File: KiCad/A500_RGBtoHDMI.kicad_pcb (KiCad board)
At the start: 2 copper layers, 80 x 29.5 mm, 13 parts, among them J1 Conn_02x20_Odd_Even, U1 Denise_Socket, U2 XC9572XL-VQ64, U3 LM1117-3.3, U4 Denise_MB_PinHeader

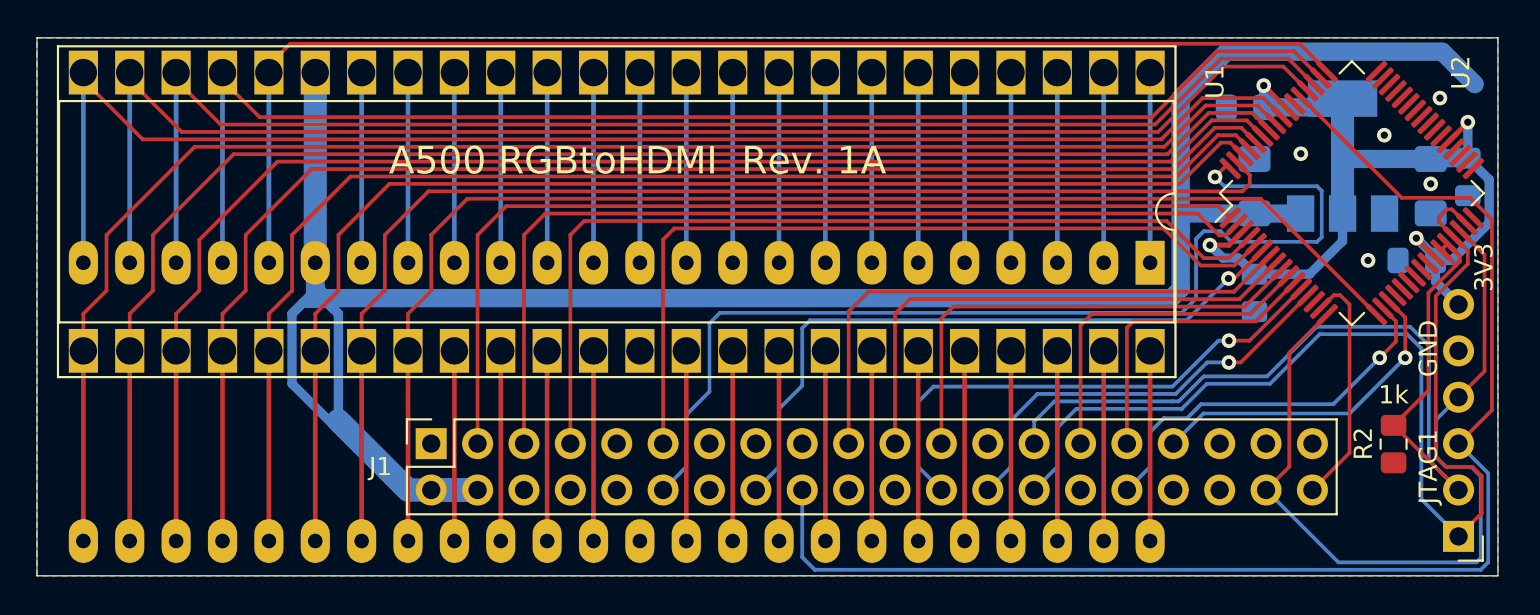
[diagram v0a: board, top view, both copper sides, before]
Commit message: added a two-pin power header VCC/GND
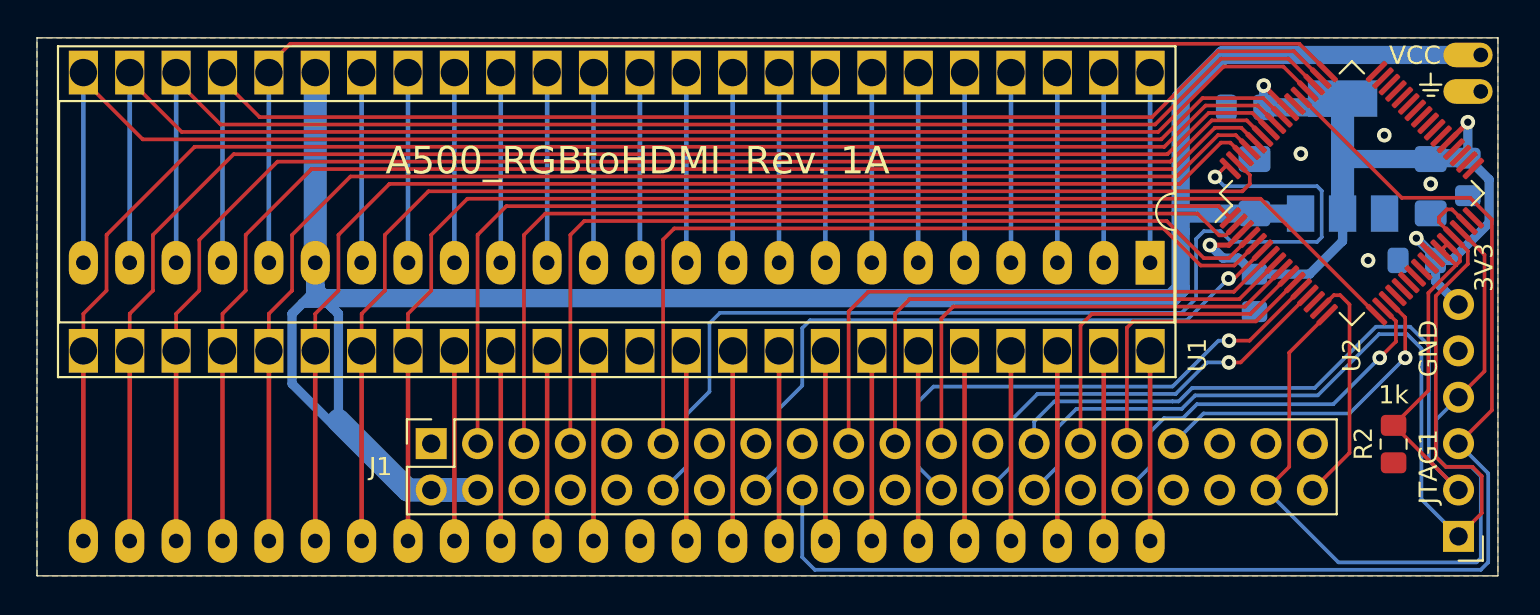
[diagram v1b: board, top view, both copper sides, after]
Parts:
- added J2: Conn_01x02, Connector_PinHeader_2.00mm:PinHeader_1x02_P2.00mm_Vertical, F.Cu at (206.1, 76.8)
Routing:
- net GND: vias 5 -> 4
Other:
- board text added: "A500_RGBtoHDMI Rev. 1A"
- board text added: "VCC"
- board text removed: "A500 RGBtoHDMI Rev. 1A"

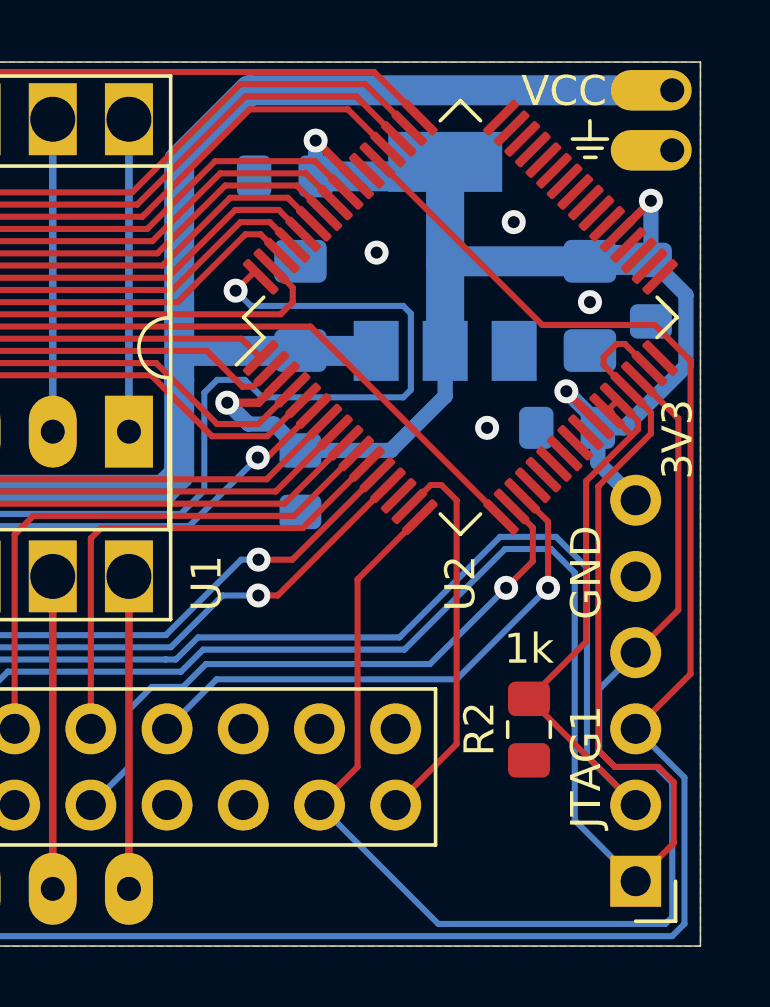
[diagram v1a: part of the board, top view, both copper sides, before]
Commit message: added Button-jumper (BT1) with 3V3-pull-up resistor
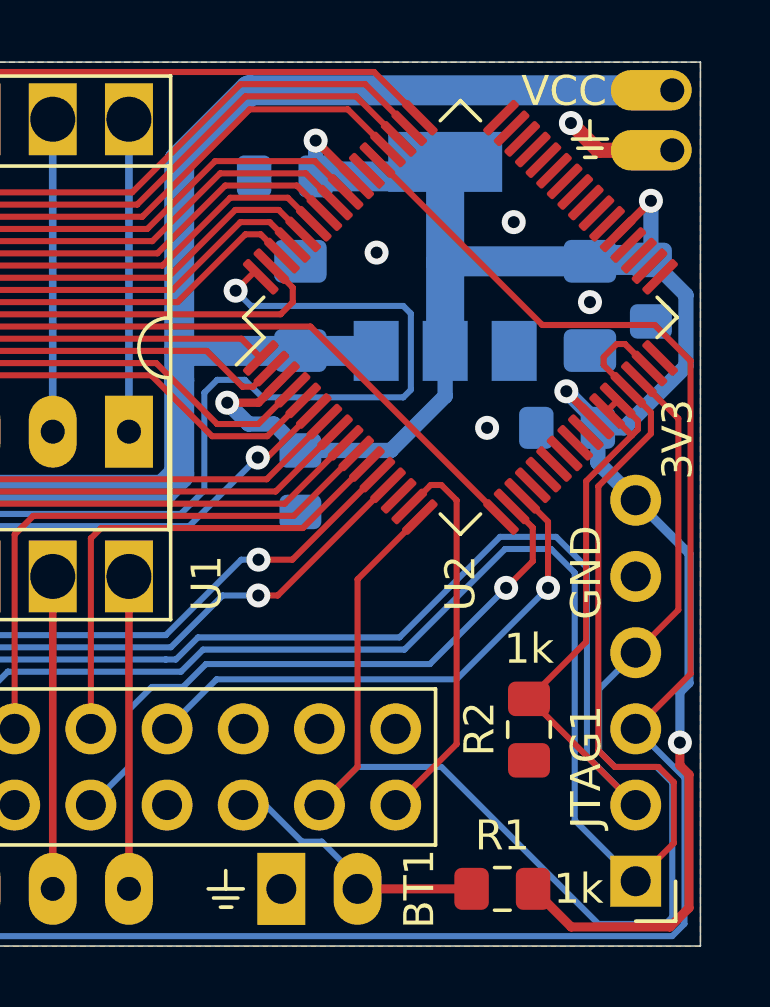
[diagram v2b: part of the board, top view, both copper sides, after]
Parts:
- added BT1: Jumper_2_Open, Connector_PinHeader_2.54mm:PinHeader_1x02_P2.54mm_Horizontal, B.Cu at (193.0, 103.4)
- added R1: 1k, Resistor_SMD:R_0805_2012Metric_Pad1.15x1.40mm_HandSolder, F.Cu at (200.4, 103.4)
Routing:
- net 3V3: track 50.5 -> 71.1 mm, vias 4 -> 5
- net Net-(BT1-Pad2): track 0.00 -> 8.99 mm
- net GND: track 0.00 -> 3.75 mm, vias 4 -> 5
- net TCK_SPCLK: track 45.9 -> 46.9 mm

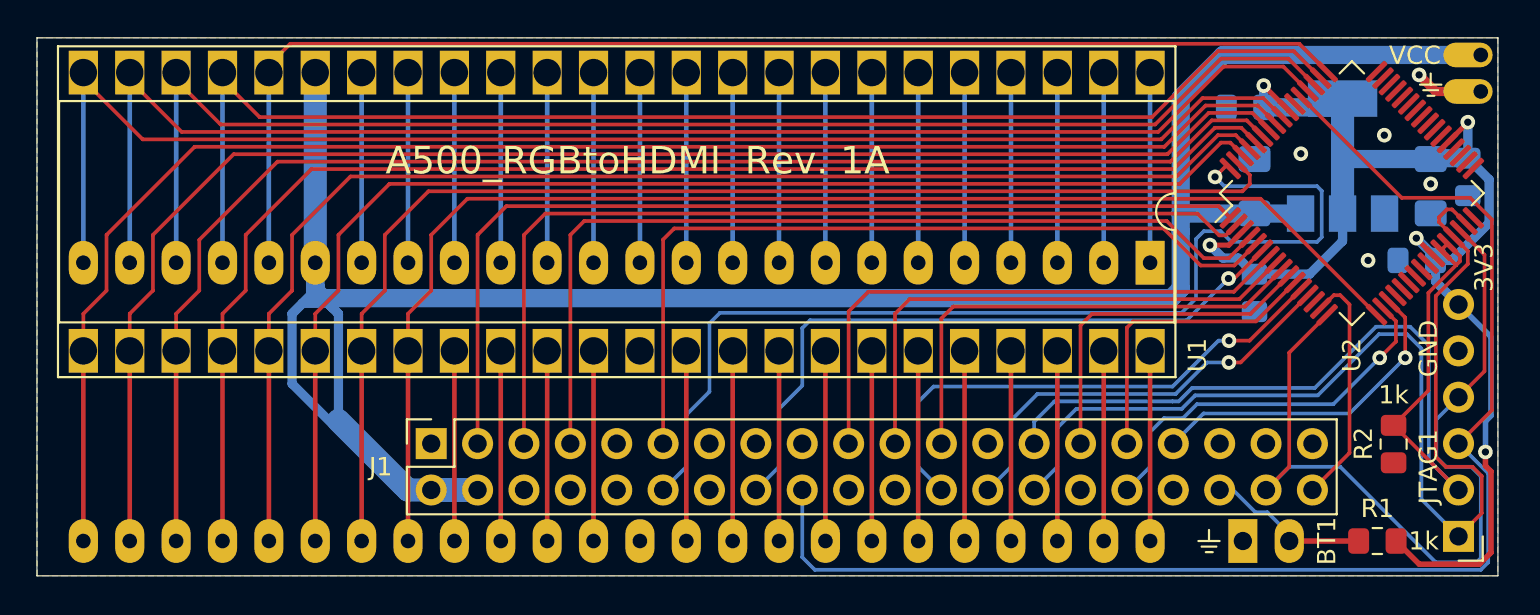
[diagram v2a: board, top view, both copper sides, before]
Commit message: added DETECT-signal with pull-down resistor
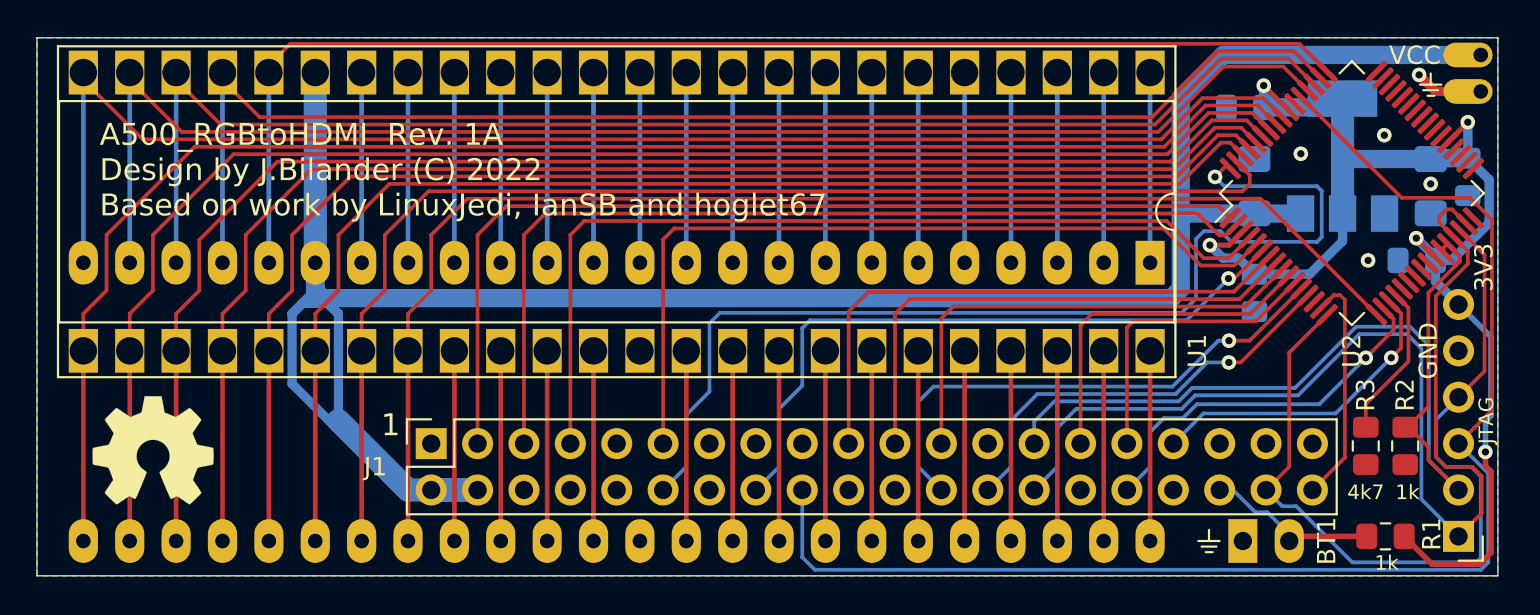
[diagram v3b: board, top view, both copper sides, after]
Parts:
- added R3: 4.7k, Resistor_SMD:R_0805_2012Metric_Pad1.15x1.40mm_HandSolder, F.Cu at (199.8, 98.2)
- added REF**: OSHW-Symbol_6.7x6mm_SilkScreen, Symbol:OSHW-Symbol_6.7x6mm_SilkScreen, B.Cu at (133.3, 98.4)
- added REF**: OSHW-Symbol_6.7x6mm_SilkScreen, Symbol:OSHW-Symbol_6.7x6mm_SilkScreen, F.Cu at (133.3, 98.4)
- moved R2 0.64 mm to (201.9, 98.2)
- moved R1 0.51 mm to (200.9, 103.1)
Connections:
- U2 pad 20: Net-(U2-Pad20) -> DETECT
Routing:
- net DETECT: track 0.00 -> 8.48 mm
- net TCK_SPCLK: track 46.9 -> 45.9 mm
- net R3_3V3: track 18.1 -> 17.4 mm
- net R2_3V3: track 21.3 -> 20.8 mm
- net Net-(BT1-Pad2): track 8.99 -> 9.54 mm
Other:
- board text added: "1"
- board text added: "4k7"
- board text added: "A500_RGBtoHDMI Rev. 1A Design by J.Bilander (C) 2022 Based on work by LinuxJedi, IanSB and hoglet67"
- board text added: "JTAG"
- board text removed: "A500_RGBtoHDMI Rev. 1A"
